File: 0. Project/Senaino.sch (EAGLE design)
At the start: 37 parts, among them Q1 16 MHz, Q2 12 MHz, U1 ATMEGA328P-PU, U3 7805T, U4 CH340G, X1 POWERSUPPLY_DC21MMX

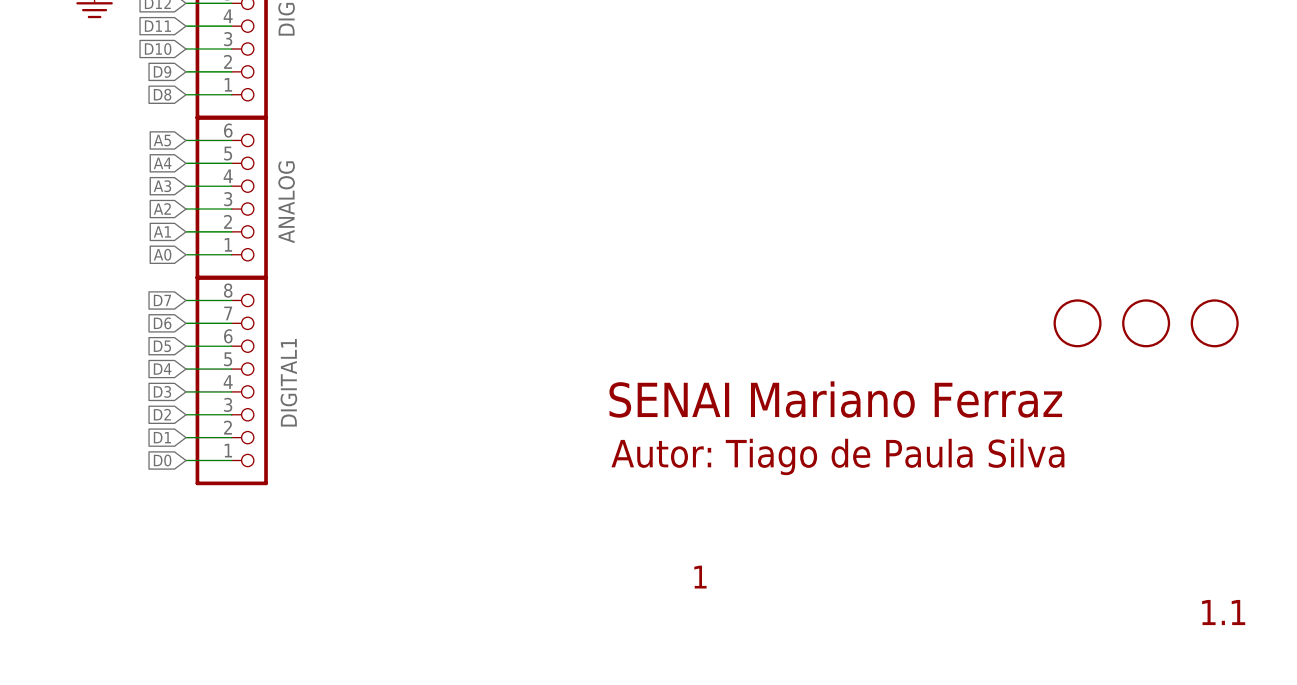
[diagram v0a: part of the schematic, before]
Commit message: Changes to CH340 performed
- Schematic OK.
- Layout OK.
- BOM OK.
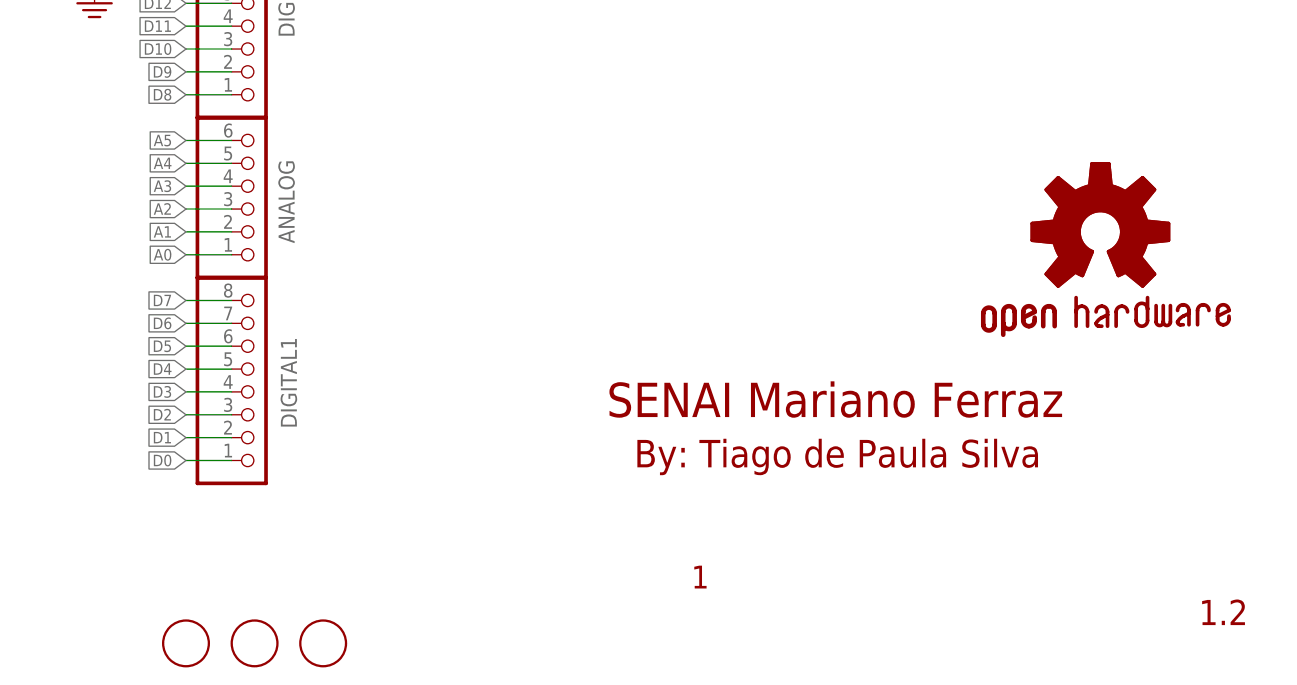
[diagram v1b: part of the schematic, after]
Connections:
- net GND: now also C15.1, C16.1
- net PE: no longer C15.1, C16.1
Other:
- note added: "1.2"
- note added: "By: Tiago de Paula Silva"
- note removed: "1.1"
- note removed: "Autor: Tiago de Paula Silva"
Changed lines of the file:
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@@
 <?xml version="1.0" encoding="utf-8"?>
 <!DOCTYPE eagle SYSTEM "eagle.dtd">
-<eagle version="9.3.0">
+<eagle version="9.4.2">
 <drawing>
 <settings>
@@
 <part name="C2" library="rcl" library_urn="urn:adsk.eagle:library:334" deviceset="C-EU" device="025-024X044" package3d_urn="urn:adsk.eagle:package:23630/1" value="100 nF"/>
 <part name="C7" library="rcl" library_urn="urn:adsk.eagle:library:334" deviceset="C-EU" device="025-024X044" package3d_urn="urn:adsk.eagle:package:23630/1" value="100 nF"/>
-<part name="R6" library="rcl" library_urn="urn:adsk.eagle:library:334" deviceset="R-EU_" device="0204/7" package3d_urn="urn:adsk.eagle:package:23498/1" value="1k"/>
-<part name="R7" library="rcl" library_urn="urn:adsk.eagle:library:334" deviceset="R-EU_" device="0204/7" package3d_urn="urn:adsk.eagle:package:23498/1" value="1k"/>
-<part name="R1" library="rcl" library_urn="urn:adsk.eagle:library:334" deviceset="R-EU_" device="0204/7" package3d_urn="urn:adsk.eagle:package:23498/1" value="330R"/>
+<part name="R6" library="rcl" library_urn="urn:adsk.eagle:library:334" deviceset="R-EU_" device="0204/7" package3d_urn="urn:adsk.eagle:package:23498/2" value="1k"/>
+<part name="R7" library="rcl" library_urn="urn:adsk.eagle:library:334" deviceset="R-EU_" device="0204/7" package3d_urn="urn:adsk.eagle:package:23498/2" value="1k"/>
+<part name="R1" library="rcl" library_urn="urn:adsk.eagle:library:334" deviceset="R-EU_" device="0204/7" package3d_urn="urn:adsk.eagle:package:23498/2" value="330R"/>
 <part name="LED1" library="led" library_urn="urn:adsk.eagle:library:259" deviceset="LED" device="3MM" package3d_urn="urn:adsk.eagle:package:15797/1"/>
 <part name="Q1" library="crystal" library_urn="urn:adsk.eagle:library:204" deviceset="CRYSTAL" device="HC49S" package3d_urn="urn:adsk.eagle:package:12071/1" value="16 MHz"/>
@@
 <part name="+5V1" library="supply2" library_urn="urn:adsk.eagle:library:372" deviceset="+5V" device=""/>
 <part name="GND2" library="supply2" library_urn="urn:adsk.eagle:library:372" deviceset="PE" device="" value="GND"/>
-<part name="R5" library="rcl" library_urn="urn:adsk.eagle:library:334" deviceset="R-EU_" device="0204/7" package3d_urn="urn:adsk.eagle:package:23498/1" value="10k"/>
+<part name="R5" library="rcl" library_urn="urn:adsk.eagle:library:334" deviceset="R-EU_" device="0204/7" package3d_urn="urn:adsk.eagle:package:23498/2" value="10k"/>
 <part name="+5V2" library="supply2" library_urn="urn:adsk.eagle:library:372" deviceset="+5V" device=""/>
-<part name="R2" library="rcl" library_urn="urn:adsk.eagle:library:334" deviceset="R-EU_" device="0204/7" package3d_urn="urn:adsk.eagle:package:23498/1" value="330R"/>
+<part name="R2" library="rcl" library_urn="urn:adsk.eagle:library:334" deviceset="R-EU_" device="0204/7" package3d_urn="urn:adsk.eagle:package:23498/2" value="330R"/>
 <part name="D3" library="diode" library_urn="urn:adsk.eagle:library:210" deviceset="1N4728" device="" package3d_urn="urn:adsk.eagle:package:43341/1"/>
 <part name="+3V3" library="supply2" library_urn="urn:adsk.eagle:library:372" deviceset="+5V" device="" value="+3.3V"/>
@@
 <part name="C3" library="rcl" library_urn="urn:adsk.eagle:library:334" deviceset="C-EU" device="025-024X044" package3d_urn="urn:adsk.eagle:package:23630/1" value="100 nF"/>
 <part name="+5V3" library="supply2" library_urn="urn:adsk.eagle:library:372" deviceset="+5V" device=""/>
-<part name="R3" library="rcl" library_urn="urn:adsk.eagle:library:334" deviceset="R-EU_" device="0204/7" package3d_urn="urn:adsk.eagle:package:23498/1" value="330R"/>
+<part name="R3" library="rcl" library_urn="urn:adsk.eagle:library:334" deviceset="R-EU_" device="0204/7" package3d_urn="urn:adsk.eagle:package:23498/2" value="330R"/>
 <part name="LED2" library="led" library_urn="urn:adsk.eagle:library:259" deviceset="LED" device="3MM" package3d_urn="urn:adsk.eagle:package:15797/1"/>
 <part name="+5V5" library="supply2" library_urn="urn:adsk.eagle:library:372" deviceset="+5V" device=""/>
-<part name="R4" library="rcl" library_urn="urn:adsk.eagle:library:334" deviceset="R-EU_" device="0204/7" package3d_urn="urn:adsk.eagle:package:23498/1" value="330R"/>
+<part name="R4" library="rcl" library_urn="urn:adsk.eagle:library:334" deviceset="R-EU_" device="0204/7" package3d_urn="urn:adsk.eagle:package:23498/2" value="330R"/>
 <part name="LED3" library="led" library_urn="urn:adsk.eagle:library:259" deviceset="LED" device="3MM" package3d_urn="urn:adsk.eagle:package:15797/1"/>
 <part name="+5V6" library="supply2" library_urn="urn:adsk.eagle:library:372" deviceset="+5V" device=""/>
@@
 <part name="GND4" library="supply2" library_urn="urn:adsk.eagle:library:372" deviceset="PE" device="" value="GND"/>
 <part name="X1" library="SmartPrj" deviceset="POWERSUPPLY_DC21MM" device="X" value=""/>
-<part name="D1" library="diode" library_urn="urn:adsk.eagle:library:210" deviceset="1N4148" device="DO35-7" package3d_urn="urn:adsk.eagle:package:43339/1" value="1N4007"/>
+<part name="D1" library="diode" library_urn="urn:adsk.eagle:library:210" deviceset="1N4148" device="DO35-7" package3d_urn="urn:adsk.eagle:package:43339/2" value="1N4007"/>
 <part name="X2" library="SmartPrj" deviceset="PN61729" device=""/>
 <part name="GND6" library="supply2" library_urn="urn:adsk.eagle:library:372" deviceset="PE" device="" value="GND"/>
 <part name="GND8" library="supply2" library_urn="urn:adsk.eagle:library:372" deviceset="PE" device="" value="GND"/>
-<part name="FD1" library="SmartPrj" deviceset="FIDUCIALMOUNT" device=""/>
 <part name="FD2" library="SmartPrj" deviceset="FIDUCIALMOUNT" device=""/>
 <part name="FD3" library="SmartPrj" deviceset="FIDUCIALMOUNT" device=""/>
@@
 <part name="GND18" library="supply2" library_urn="urn:adsk.eagle:library:372" deviceset="PE" device="" value="GND"/>
 <part name="GND7" library="supply2" library_urn="urn:adsk.eagle:library:372" deviceset="PE" device="" value="GND"/>
+<part name="FD1" library="SmartPrj" deviceset="FIDUCIALMOUNT" device=""/>
+<part name="GOLD_ORB_SM1" library="OSHW" deviceset="OSHWLOGO" device=""/>
 </parts>
 <sheets>
@@
 <plain>
 <text x="188.976" y="30.226" size="3.81" layer="94">SENAI Mariano Ferraz</text>
-<text x="189.484" y="24.638" size="3.048" layer="94">Autor: Tiago de Paula Silva</text>
-<text x="254.762" y="7.112" size="2.794" layer="94">1.1</text>
+<text x="192.024" y="24.638" size="3.048" layer="94">By: Tiago de Paula Silva</text>
+<text x="254.762" y="7.112" size="2.794" layer="94">1.2</text>
 <text x="198.374" y="11.176" size="2.54" layer="94">1</text>
 </plain>
@@
 <attribute name="VALUE" x="257.175" y="107.061" size="1.778" layer="96" display="off"/>
 </instance>
-<instance part="FD1" gate="G$1" x="241.3" y="40.64" smashed="yes"/>
-<instance part="FD2" gate="G$1" x="248.92" y="40.64" smashed="yes"/>
-<instance part="FD3" gate="G$1" x="256.54" y="40.64" smashed="yes"/>
+<instance part="FD2" gate="G$1" x="149.86" y="5.08" smashed="yes"/>
+<instance part="FD3" gate="G$1" x="157.48" y="5.08" smashed="yes"/>
 <instance part="POWER" gate="A" x="149.86" y="101.6" smashed="yes">
 <attribute name="NAME" x="154.305" y="97.79" size="1.778" layer="95" rot="R90"/>
@@
 <attribute name="VALUE" x="201.295" y="91.821" size="1.778" layer="96" display="off"/>
 </instance>
+<instance part="FD1" gate="G$1" x="142.24" y="5.08" smashed="yes"/>
+<instance part="GOLD_ORB_SM1" gate="G$1" x="243.84" y="50.8" smashed="yes"/>
 </instances>
 <busses>
@@
 <wire x1="40.64" y1="20.32" x2="40.64" y2="38.1" width="0.1524" layer="91"/>
 </segment>
+<segment>
+<pinref part="C15" gate="G$1" pin="1"/>
+<wire x1="182.88" y1="109.22" x2="182.88" y2="101.6" width="0.1524" layer="91"/>
+<pinref part="C16" gate="G$1" pin="1"/>
+<wire x1="193.04" y1="101.6" x2="193.04" y2="109.22" width="0.1524" layer="91"/>
+<wire x1="182.88" y1="101.6" x2="187.96" y2="101.6" width="0.1524" layer="91"/>
+<pinref part="GND18" gate="PE" pin="PE"/>
+<wire x1="187.96" y1="101.6" x2="193.04" y2="101.6" width="0.1524" layer="91"/>
+<wire x1="187.96" y1="99.06" x2="187.96" y2="101.6" width="0.1524" layer="91"/>
+<junction x="187.96" y="101.6"/>
+</segment>
 </net>
 <net name="D1" class="0">
@@
 <net name="PE" class="0">
 <segment>
-<pinref part="C15" gate="G$1" pin="1"/>
-<wire x1="182.88" y1="109.22" x2="182.88" y2="101.6" width="0.1524" layer="91"/>
-<pinref part="C16" gate="G$1" pin="1"/>
-<wire x1="193.04" y1="101.6" x2="193.04" y2="109.22" width="0.1524" layer="91"/>
-<wire x1="182.88" y1="101.6" x2="187.96" y2="101.6" width="0.1524" layer="91"/>
-<pinref part="GND18" gate="PE" pin="PE"/>
-<wire x1="187.96" y1="101.6" x2="193.04" y2="101.6" width="0.1524" layer="91"/>
-<wire x1="187.96" y1="99.06" x2="187.96" y2="101.6" width="0.1524" layer="91"/>
-<junction x="187.96" y="101.6"/>
-</segment>
-<segment>
 <pinref part="U4" gate="U1" pin="GND"/>

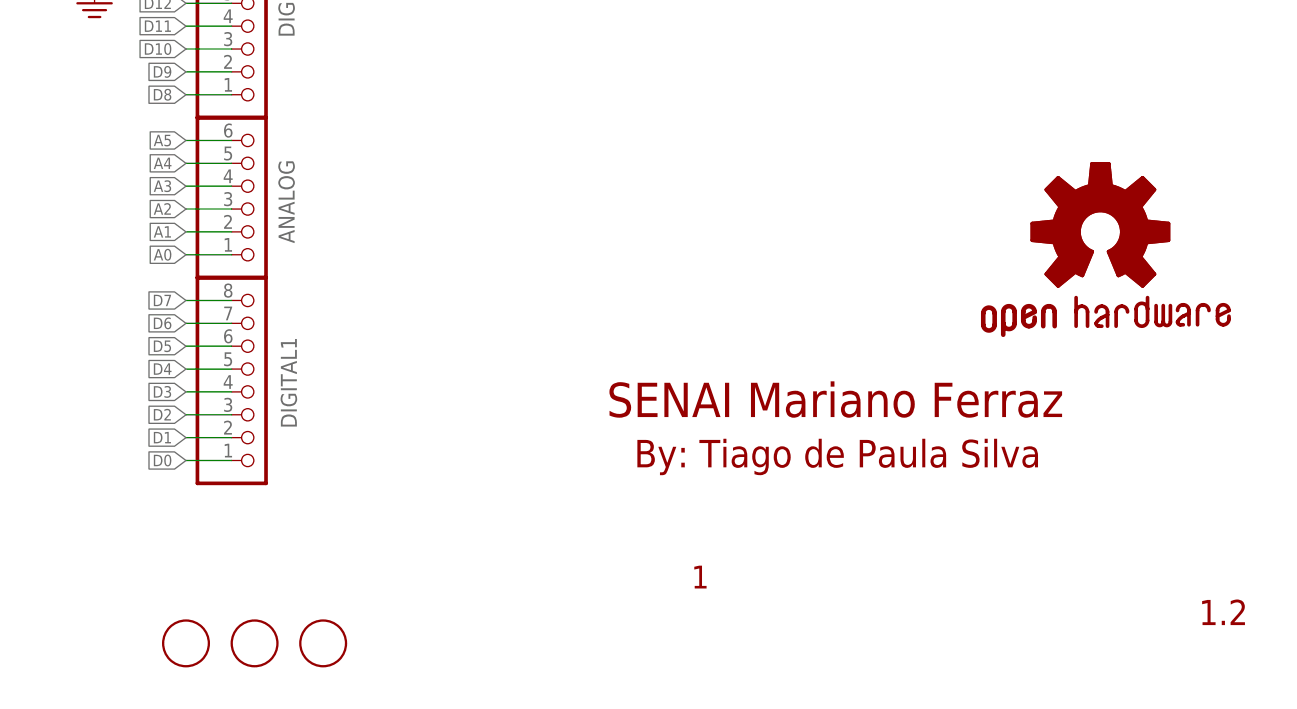
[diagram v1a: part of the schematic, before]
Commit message: Frame schematic updated
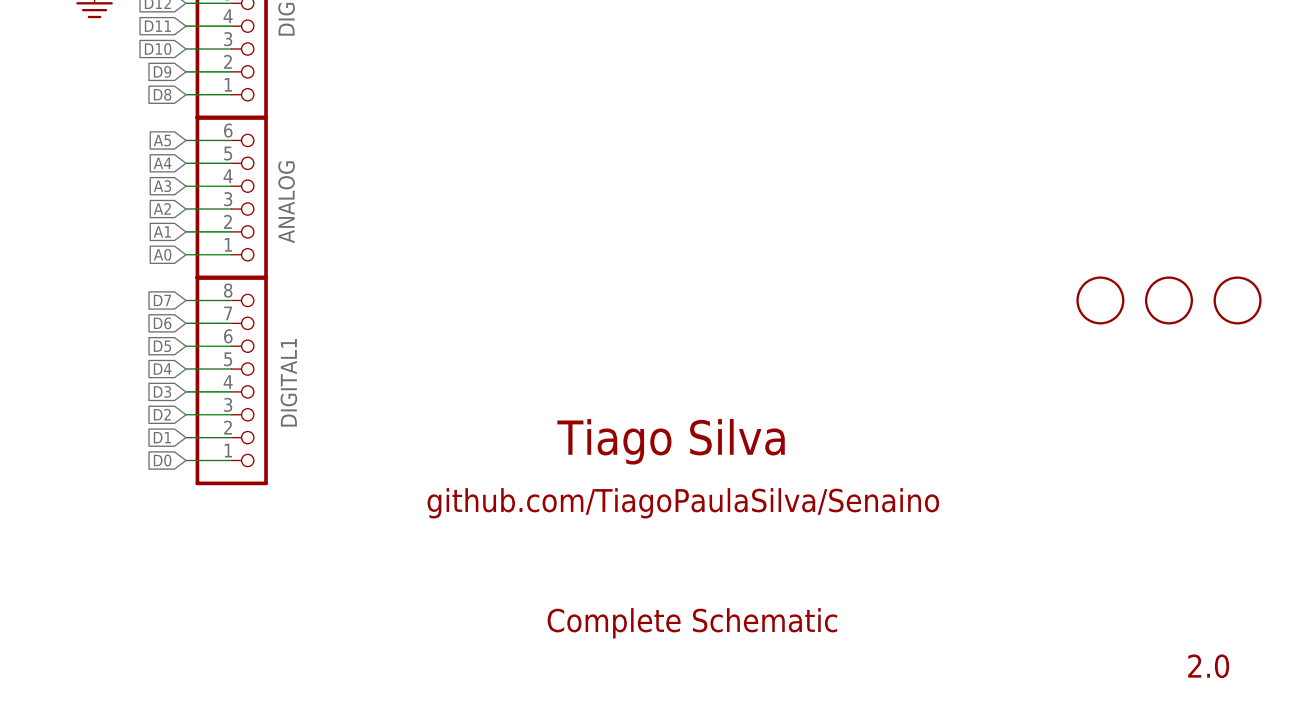
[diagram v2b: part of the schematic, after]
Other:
- note added: "2.0"
- note added: "Complete Schematic"
- note added: "Tiago Silva"
- note added: "github.com/TiagoPaulaSilva/Senaino"
- note removed: "1"
- note removed: "1.2"
- note removed: "By: Tiago de Paula Silva"
- note removed: "SENAI Mariano Ferraz"
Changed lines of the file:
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@@
 <layer number="59" name="tCarbon" color="7" fill="1" visible="no" active="no"/>
 <layer number="60" name="bCarbon" color="7" fill="1" visible="no" active="no"/>
+<layer number="88" name="SimResults" color="9" fill="1" visible="yes" active="yes"/>
+<layer number="89" name="SimProbes" color="9" fill="1" visible="yes" active="yes"/>
 <layer number="90" name="Modules" color="5" fill="1" visible="yes" active="yes"/>
 <layer number="91" name="Nets" color="2" fill="1" visible="yes" active="yes"/>
@@
 <layer number="230" name="230bmp" color="7" fill="1" visible="yes" active="yes"/>
 <layer number="231" name="231bmp" color="7" fill="1" visible="yes" active="yes"/>
+<layer number="232" name="Eagle3D_PG2" color="7" fill="1" visible="no" active="no"/>
+<layer number="233" name="Eagle3D_PG3" color="7" fill="1" visible="no" active="no"/>
 <layer number="248" name="Housing" color="7" fill="1" visible="yes" active="yes"/>
 <layer number="249" name="Edge" color="7" fill="1" visible="yes" active="yes"/>
@@
 </classes>
 <parts>
-<part name="FRAME1" library="frames" library_urn="urn:adsk.eagle:library:229" deviceset="DINA4_L" device=""/>
 <part name="U1" library="SmartPrj" deviceset="ATMEGA328P-" device="PU"/>
 <part name="U3" library="linear" library_urn="urn:adsk.eagle:library:262" deviceset="78*" device="T" package3d_urn="urn:adsk.eagle:package:16414/1" technology="05"/>
@@
 <part name="GND7" library="supply2" library_urn="urn:adsk.eagle:library:372" deviceset="PE" device="" value="GND"/>
 <part name="FD1" library="SmartPrj" deviceset="FIDUCIALMOUNT" device=""/>
-<part name="GOLD_ORB_SM1" library="OSHW" deviceset="OSHWLOGO" device=""/>
+<part name="FRAME1" library="frames" deviceset="DINA4_L" device=""/>
 </parts>
 <sheets>
 <sheet>
 <plain>
-<text x="188.976" y="30.226" size="3.81" layer="94">SENAI Mariano Ferraz</text>
-<text x="192.024" y="24.638" size="3.048" layer="94">By: Tiago de Paula Silva</text>
-<text x="254.762" y="7.112" size="2.794" layer="94">1.2</text>
-<text x="198.374" y="11.176" size="2.54" layer="94">1</text>
+<text x="183.515" y="26.035" size="3.81" layer="94">Tiago Silva</text>
+<text x="168.91" y="19.685" size="2.54" layer="94">github.com/TiagoPaulaSilva/Senaino</text>
+<text x="253.365" y="1.27" size="2.54" layer="94" ratio="5">2.0</text>
+<text x="182.245" y="6.35" size="2.54" layer="94" ratio="5">Complete Schematic</text>
 </plain>
 <instances>
-<instance part="FRAME1" gate="G$1" x="0" y="0" smashed="yes"/>
-<instance part="FRAME1" gate="G$2" x="162.56" y="0" smashed="yes">
-<attribute name="LAST_DATE_TIME" x="175.26" y="1.27" size="2.54" layer="94"/>
-<attribute name="SHEET" x="248.92" y="1.27" size="2.54" layer="94"/>
-<attribute name="DRAWING_NAME" x="180.34" y="19.05" size="2.54" layer="94"/>
-</instance>
 <instance part="U1" gate="G$1" x="76.2" y="53.34" smashed="yes">
 <attribute name="VALUE" x="60.96" y="20.32" size="1.778" layer="96"/>
@@
 <attribute name="VALUE" x="257.175" y="107.061" size="1.778" layer="96" display="off"/>
 </instance>
-<instance part="FD2" gate="G$1" x="149.86" y="5.08" smashed="yes"/>
-<instance part="FD3" gate="G$1" x="157.48" y="5.08" smashed="yes"/>
+<instance part="FD2" gate="G$1" x="251.46" y="43.18" smashed="yes"/>
+<instance part="FD3" gate="G$1" x="259.08" y="43.18" smashed="yes"/>
 <instance part="POWER" gate="A" x="149.86" y="101.6" smashed="yes">
 <attribute name="NAME" x="154.305" y="97.79" size="1.778" layer="95" rot="R90"/>
@@
 <attribute name="VALUE" x="201.295" y="91.821" size="1.778" layer="96" display="off"/>
 </instance>
-<instance part="FD1" gate="G$1" x="142.24" y="5.08" smashed="yes"/>
-<instance part="GOLD_ORB_SM1" gate="G$1" x="243.84" y="50.8" smashed="yes"/>
+<instance part="FD1" gate="G$1" x="243.84" y="43.18" smashed="yes"/>
+<instance part="FRAME1" gate="G$1" x="0" y="0" smashed="yes"/>
+<instance part="FRAME1" gate="G$2" x="162.56" y="0" smashed="yes">
+<attribute name="LAST_DATE_TIME" x="173.99" y="1.27" size="2.54" layer="94"/>
+<attribute name="SHEET" x="255.27" y="6.35" size="2.54" layer="94"/>
+<attribute name="DRAWING_NAME" x="187.96" y="11.557" size="2.54" layer="94"/>
+</instance>
 </instances>
 <busses>
